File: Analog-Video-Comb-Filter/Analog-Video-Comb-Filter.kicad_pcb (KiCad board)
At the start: 2 copper layers, 51.5 x 104.1 mm, 80 parts, among them J1 12VDC(+), J2 SVHS, J3 CV-OUT, J4 CV-IN, Q1 BC548, U1 L7805, U2 AD8044, U3 SAA4960/61, U4 MC44144, U5 74HC04, U6 LM1881, U7 SAA4963, Y1 See table

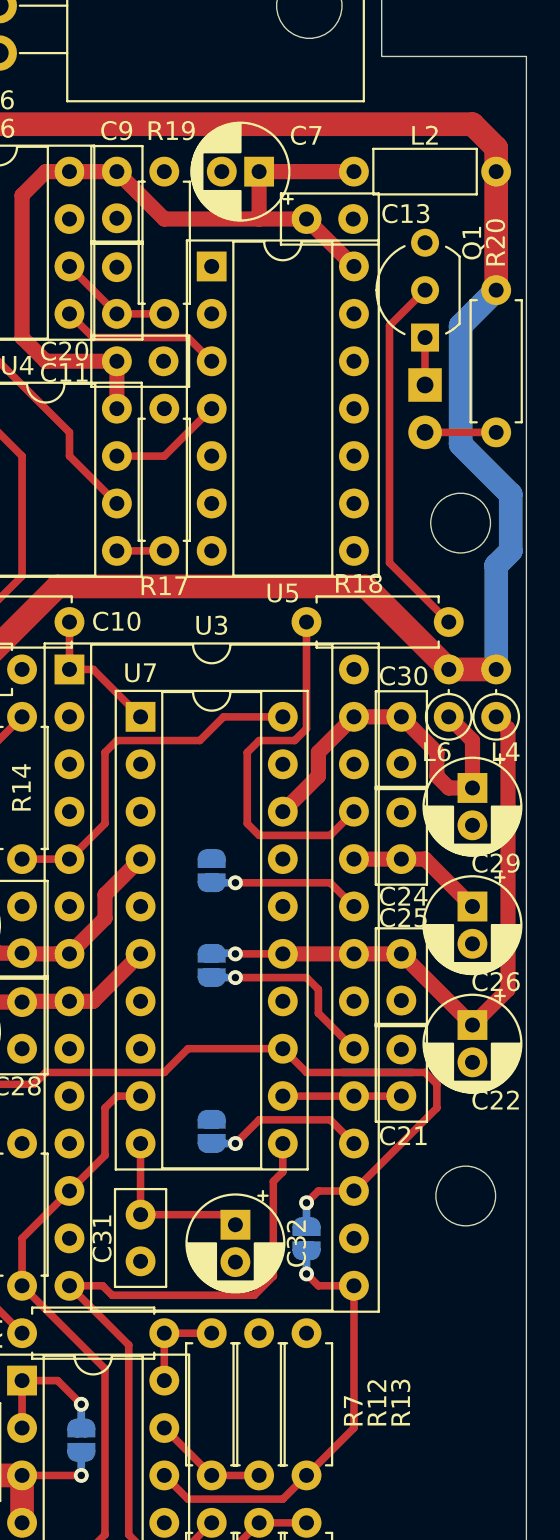
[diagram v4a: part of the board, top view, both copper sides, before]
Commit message: Fixed numbering mistakes on PCB, fixed BOM, added color comparison images
- Fixed incorrect R12, R13, R18 and R19 numbers on PCB.
- Removed 560 ohm resistors from parts list.
- Changed 2.2k resistor to 1k as its resistance wasn't critical, now there's one less different part.
- Set solder jumpers and some mutually exclusive parts to be excluded from BOM generation.
- Renamed documentation folder to pdf.
- Added PCB layers in PDF form.
- Added color comparison images, and moved the monochrome comparison images to a collapsible section.
- Added rev.2 assembled PCB photo.
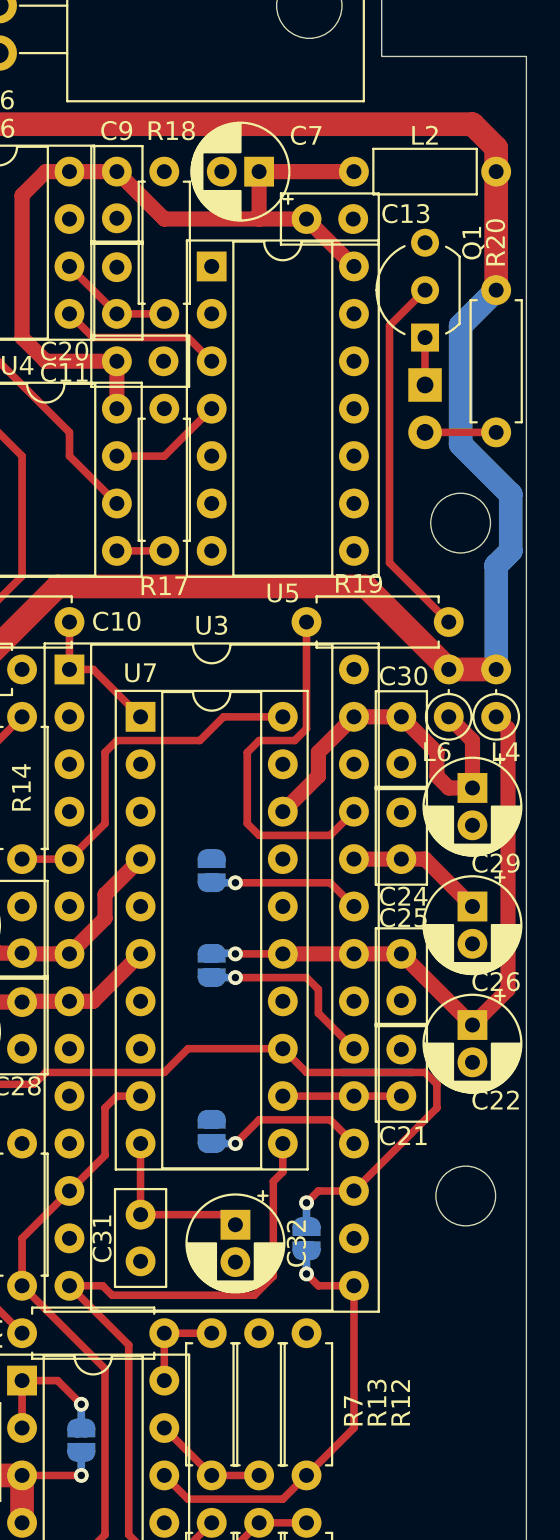
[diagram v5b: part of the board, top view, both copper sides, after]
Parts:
- R19: renamed from R18; value 2,2k -> 1k
- renumbered R19 to R18
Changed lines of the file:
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@@
   (paper "A4")
   (title_block
-    (title "SAA4960 / SAA4961 Analog Video Comb Filter")
-    (date "2026-02-14")
+    (title "SAA4960 / SAA4961 / SAA4963 Analog Video Comb Filter")
+    (date "2026-02-21")
     (rev "2")
     (company "github.com/goscickiw")
@@
     (property "Sheetfile" "Analog-Video-Comb-Filter.kicad_sch")
     (property "Sheetname" "")
+    (property "exclude_from_bom" "")
     (property "ki_description" "Integrated NTSC comb filter")
     (property "ki_keywords" "NTSC comb filter luminance chrominance")
-    (attr through_hole)
+    (attr through_hole exclude_from_bom)
     (fp_text reference "U7" (at 0 -2.33) (layer "F.SilkS")
         (effects (font (size 1 1) (thickness 0.15)))
@@
     (property "Sheetfile" "Analog-Video-Comb-Filter.kicad_sch")
     (property "Sheetname" "")
+    (property "exclude_from_bom" "")
     (property "ki_description" "Unpolarized capacitor")
     (property "ki_keywords" "cap capacitor")
-    (attr through_hole)
+    (attr through_hole exclude_from_bom)
     (fp_text reference "C31" (at 1.27 2.032 90) (layer "F.SilkS")
         (effects (font (size 1 1) (thickness 0.15)))
@@
     (property "Sheetfile" "Analog-Video-Comb-Filter.kicad_sch")
     (property "Sheetname" "")
+    (property "exclude_from_bom" "")
     (property "ki_description" "Polarized capacitor")
     (property "ki_keywords" "cap capacitor")
-    (attr through_hole)
+    (attr through_hole exclude_from_bom)
     (fp_text reference "C32" (at 0.984 -3.302 90) (layer "F.SilkS")
         (effects (font (size 1 1) (thickness 0.15)))
@@
     (property "ki_keywords" "R res resistor")
     (attr through_hole)
-    (fp_text reference "R13" (at 2.54 7.62 90) (layer "F.SilkS")
+    (fp_text reference "R13" (at 2.54 6.35 90) (layer "F.SilkS")
         (effects (font (size 1 1) (thickness 0.15)) (justify left))
     )
@@
     (property "ki_keywords" "R res resistor")
     (attr through_hole)
-    (fp_text reference "R19" (at -2.159 -0.381 -180) (layer "F.SilkS")
+    (fp_text reference "R18" (at -2.159 -0.381 -180) (layer "F.SilkS")
         (effects (font (size 1 1) (thickness 0.15)))
     )
@@
     (property "ki_keywords" "R res resistor")
     (attr through_hole)
-    (fp_text reference "R18" (at 2.794 -2.032) (layer "F.SilkS")
+    (fp_text reference "R19" (at 2.794 -2.032) (layer "F.SilkS")
         (effects (font (size 1 1) (thickness 0.15)))
     )
-    (fp_text value "2,2k" (at 3.81 2.37) (layer "F.Fab")
+    (fp_text value "1k" (at 3.81 2.37) (layer "F.Fab")
         (effects (font (size 1 1) (thickness 0.15)))
     )
@@
     (property "ki_keywords" "R res resistor")
     (attr through_hole)
-    (fp_text reference "R12" (at 2.54 3.81 90) (layer "F.SilkS")
+    (fp_text reference "R12" (at 2.54 5.08 90) (layer "F.SilkS")
         (effects (font (size 1 1) (thickness 0.15)) (justify left))
     )
@@
     (property "Sheetfile" "Analog-Video-Comb-Filter.kicad_sch")
     (property "Sheetname" "")
+    (property "exclude_from_bom" "")
     (property "ki_description" "Solder Jumper, 2-pole, open")
     (property "ki_keywords" "solder jumper SPST")
-    (attr exclude_from_pos_files)
+    (attr exclude_from_pos_files exclude_from_bom)
     (fp_text reference "JP2" (at 0 1.8 90) (layer "B.Fab")
         (effects (font (size 1 1) (thickness 0.15)) (justify mirror))
@@
     (property "Sheetfile" "Analog-Video-Comb-Filter.kicad_sch")
     (property "Sheetname" "")
+    (property "exclude_from_bom" "")
     (property "ki_description" "Solder Jumper, 2-pole, open")
     (property "ki_keywords" "solder jumper SPST")
-    (attr exclude_from_pos_files)
+    (attr exclude_from_pos_files exclude_from_bom)
     (fp_text reference "JP1" (at 0 1.8 90) (layer "B.SilkS") hide
         (effects (font (size 1 1) (thickness 0.15)) (justify mirror))
@@
     (property "Sheetfile" "Analog-Video-Comb-Filter.kicad_sch")
     (property "Sheetname" "")
+    (property "exclude_from_bom" "")
     (property "ki_description" "Solder Jumper, 2-pole, open")
     (property "ki_keywords" "solder jumper SPST")
-    (attr exclude_from_pos_files)
+    (attr exclude_from_pos_files exclude_from_bom)
     (fp_text reference "JP5" (at 0 1.8 90) (layer "B.SilkS") hide
         (effects (font (size 1 1) (thickness 0.15)) (justify mirror))
@@
     (property "Sheetfile" "Analog-Video-Comb-Filter.kicad_sch")
     (property "Sheetname" "")
+    (property "exclude_from_bom" "")
     (property "ki_description" "Solder Jumper, 2-pole, open")
     (property "ki_keywords" "solder jumper SPST")
-    (attr exclude_from_pos_files)
+    (attr exclude_from_pos_files exclude_from_bom)
     (fp_text reference "JP4" (at 0 1.8 90) (layer "B.Fab")
         (effects (font (size 1 1) (thickness 0.15)) (justify mirror))
@@
     (property "Sheetfile" "Analog-Video-Comb-Filter.kicad_sch")
     (property "Sheetname" "")
+    (property "exclude_from_bom" "")
     (property "ki_description" "Solder Jumper, 2-pole, open")
     (property "ki_keywords" "solder jumper SPST")
-    (attr exclude_from_pos_files)
+    (attr exclude_from_pos_files exclude_from_bom)
     (fp_text reference "JP3" (at 0 1.8 90) (layer "B.Fab")
         (effects (font (size 1 1) (thickness 0.15)) (justify mirror))
